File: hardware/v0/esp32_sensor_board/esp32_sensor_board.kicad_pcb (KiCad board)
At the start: 4 copper layers, 76 x 62 mm, 70 parts, among them J101 Conn_01x02, J102 Conn_01x02, J301 USB_B_Micro, J302 Micro_SD_Card_Det, J303 Conn_Coaxial, J501 Conn_01x05, J502 Conn_01x05, SW301 SW_SPST, U201 LMR36006, U302 ESP32-C3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

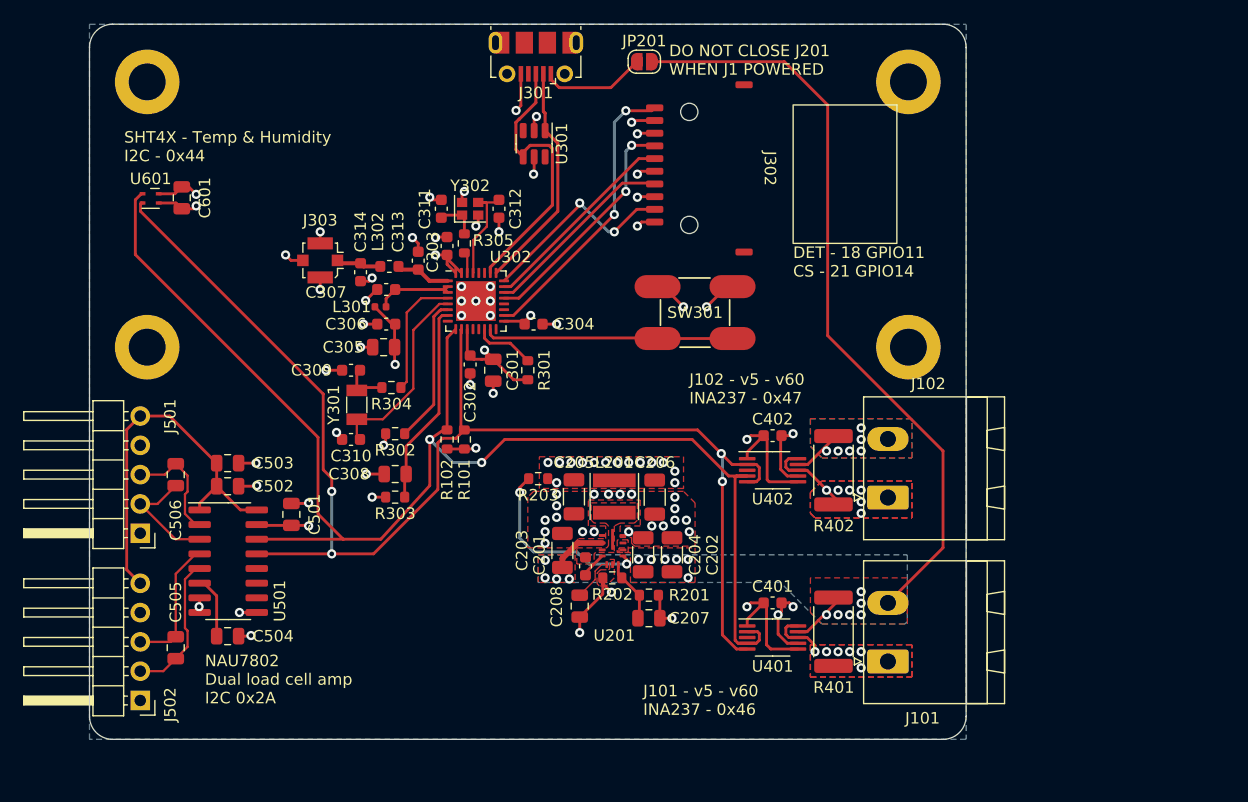
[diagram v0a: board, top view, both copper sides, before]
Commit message: Board refactor WIP.  Still needs PU resistors
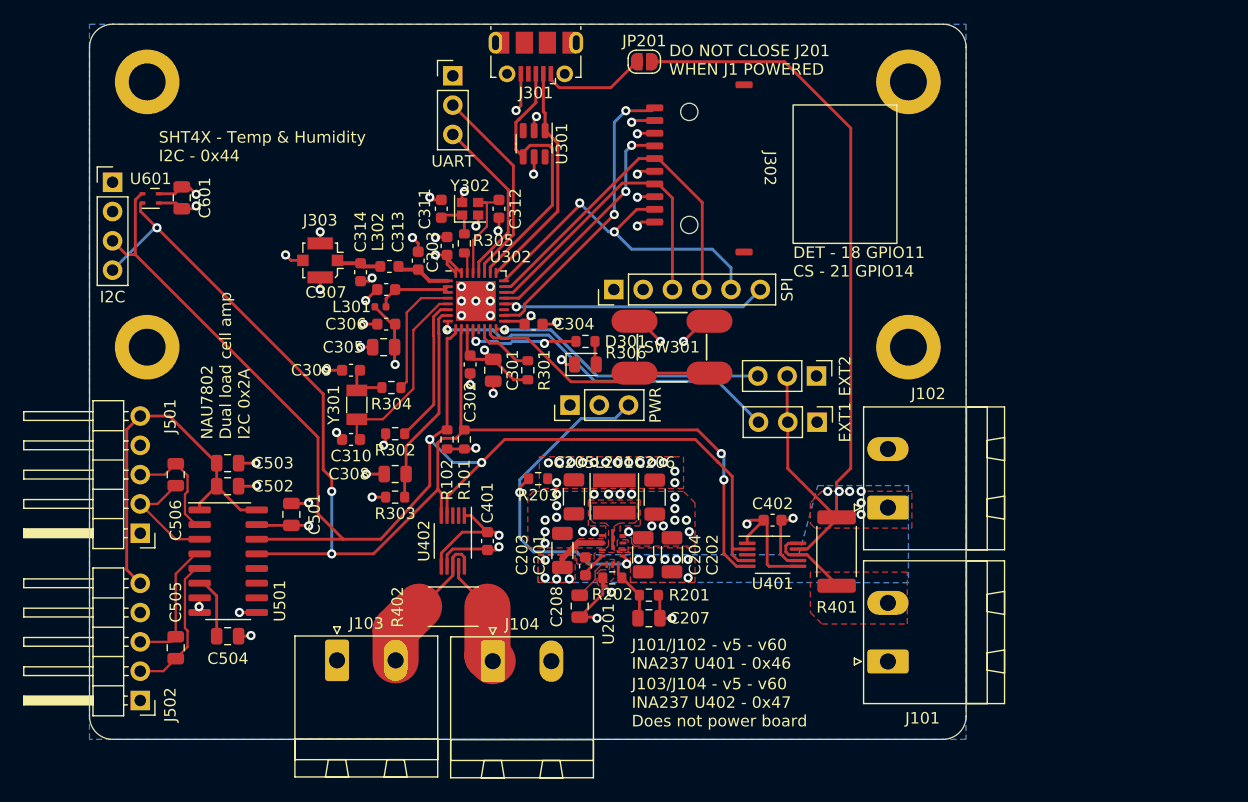
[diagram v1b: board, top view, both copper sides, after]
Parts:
- removed the G*** at (109.5, 127.0)
- added D301: STATUS_LED, LED_SMD:LED_0805_2012Metric, F.Cu at (128.5, 99.5)
- added J103: Conn_01x02, Connector_Phoenix_MSTB:PhoenixContact_MSTBA_2,5_2-G-5,08_1x02_P5.08mm_Horizontal, F.Cu at (107.0, 125.2)
- added J104: Conn_01x02, Connector_Phoenix_MSTB:PhoenixContact_MSTBA_2,5_2-G-5,08_1x02_P5.08mm_Horizontal, F.Cu at (120.5, 125.2)
- added J201: PWR, Connector_PinHeader_2.54mm:PinHeader_1x03_P2.54mm_Vertical, F.Cu at (127.2, 103.0)
- added J304: UART, Connector_PinHeader_2.54mm:PinHeader_1x03_P2.54mm_Vertical, F.Cu at (117.0, 74.5)
- added J305: EXT1, Connector_PinHeader_2.54mm:PinHeader_1x03_P2.54mm_Vertical, F.Cu at (148.6, 104.5)
- added J306: EXT2, Connector_PinHeader_2.54mm:PinHeader_1x03_P2.54mm_Vertical, F.Cu at (148.5, 100.5)
- added J307: I2C, Connector_PinHeader_2.54mm:PinHeader_1x04_P2.54mm_Vertical, F.Cu at (87.5, 83.7)
- added J308: SPI, Connector_PinHeader_2.54mm:PinHeader_1x06_P2.54mm_Vertical, F.Cu at (131.0, 93.0)
- added R306: R_Small, Resistor_SMD:R_0603_1608Metric, F.Cu at (128.5, 97.5)
- moved R402 35.0 mm to (117.0, 120.5), turned to 0 degrees
- moved U402 29.0 mm to (117.0, 114.8), turned to -90 degrees
- moved C401 25.3 mm to (120.0, 114.8), turned to -90 degrees
- moved G*** 21.4 mm to (112.5, 100.0)
- moved C402 7.33 mm to (144.7, 113.0)
- moved U401 7.33 mm to (144.7, 116.0)
- moved R401 6.96 mm to (150.3, 115.7)
- moved SW301 3.61 mm to (136.0, 98.0)
- moved J102 0.87 mm to (154.7, 111.9)
- renumbered U402 to U401, U401 to U402
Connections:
- J101 pad 1: /Vbus1_in -> GND
- J101 pad 2: VIN -> /Vbus1_in
- J102 pad 1: /Vbus2_in -> VIN
- J102 pad 2: /Vbus2_out -> GND
- U302 pad 12: unconnected-(U302-MTCK/GPIO6-Pad12) -> /Microprocessor/STATUS_LED
- U302 pad 13: unconnected-(U302-MTDO/GPIO7-Pad13) -> /Load Cell Sensor/DRDY_NAU
- U302 pad 16: unconnected-(U302-GPIO10-Pad16) -> /Microprocessor/EXT_2
- U302 pad 20: unconnected-(U302-SPIWP/GPIO13-Pad20) -> /Microprocessor/SPI_CS1
- U302 pad 27: unconnected-(U302-U0RXD/GPIO20-Pad27) -> /Microprocessor/UART_RX
- U302 pad 28: unconnected-(U302-U0TXD/GPIO21-Pad28) -> /Microprocessor/UART_TX
- U302 pad 8: unconnected-(U302-GPIO3/ADC1_CH3-Pad8) -> /Microprocessor/EXT_1
- U401 pad 10: /Vbus2_in -> /Vbus1_in
- U401 pad 2: /Power Measurement/I2C_SCL -> /Power Measurement/I2C_SDA
- U401 pad 8: /Vbus2_in -> /Vbus1_in
- U401 pad 9: /Vbus2_out -> VIN
- U402 pad 10: /Vbus1_in -> /Vbus2_in
- U402 pad 2: /Power Measurement/I2C_SDA -> /Power Measurement/I2C_SCL
- U402 pad 8: /Vbus1_in -> /Vbus2_in
- U402 pad 9: VIN -> /Vbus2_out
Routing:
- net /Microprocessor/EXT_1: track 0.00 -> 31.3 mm, vias 0 -> 1
- net /Microprocessor/EXT_2: track 0.00 -> 24.4 mm, vias 0 -> 1
- net /Microprocessor/SPI_CS1: track 0.00 -> 22.9 mm, vias 0 -> 1
- net /Microprocessor/UART_RX: track 0.00 -> 17.8 mm
- net /Microprocessor/UART_TX: track 0.00 -> 15.1 mm
- net /Microprocessor/SPI_CIPO: track 17.8 -> 31.1 mm
- net /Microprocessor/SPI_COPI: track 17.7 -> 30.9 mm
- net P_GOOD: track 16.5 -> 29.7 mm
- net /Microprocessor/STATUS_LED: track 0.00 -> 10.1 mm, vias 0 -> 2
- net /Microprocessor/SPI_SCK: track 17.0 -> 27.0 mm
- net /Vbus2_in: track 7.61 -> 13.1 mm, vias 6 -> 0
- net /Power Measurement/I2C_SCL: track 118.6 -> 113.2 mm, vias 4 -> 5
- net /Vbus2_out: track 4.35 -> 9.45 mm, vias 6 -> 0
- net /Power Measurement/I2C_SDA: track 119.3 -> 116.9 mm
- net /Vbus1_in: track 5.24 -> 7.35 mm, vias 6 -> 0
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- removed copper zone on B.Cu, net /Vbus1_in
- removed copper zone on B.Cu, net /Vbus2_in
- removed copper zone on F.Cu, net /Vbus2_in
- removed copper zone on B.Cu, net /Vbus2_out
- removed copper zone on F.Cu, net /Vbus2_out
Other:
- board text added: "ESP32-C3FH4 sensor board v5 - v60 input on J101 - Powers board v5 - v60 measurement on J103 +V is always the inside pin of each pair v0.2 Prototype - 2023-Oct-04 AB4EN"
- board text added: "J101/J102 - v5 - v60 INA237 U401 - 0x46"
- board text added: "J103/J104 - v5 - v60 INA237 U402 - 0x47 Does not power board"
- board text removed: "ESP32-C3FH4 sensor board v5 - v60 input on J101 - Powers board v5 - v60 measurement on J102 v0.1 Prototype - 2023-Jul-31"
- board text removed: "J101 - v5 - v60 INA237 - 0x46"
- board text removed: "J102 - v5 - v60 INA237 - 0x47"

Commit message: TVS and PU work
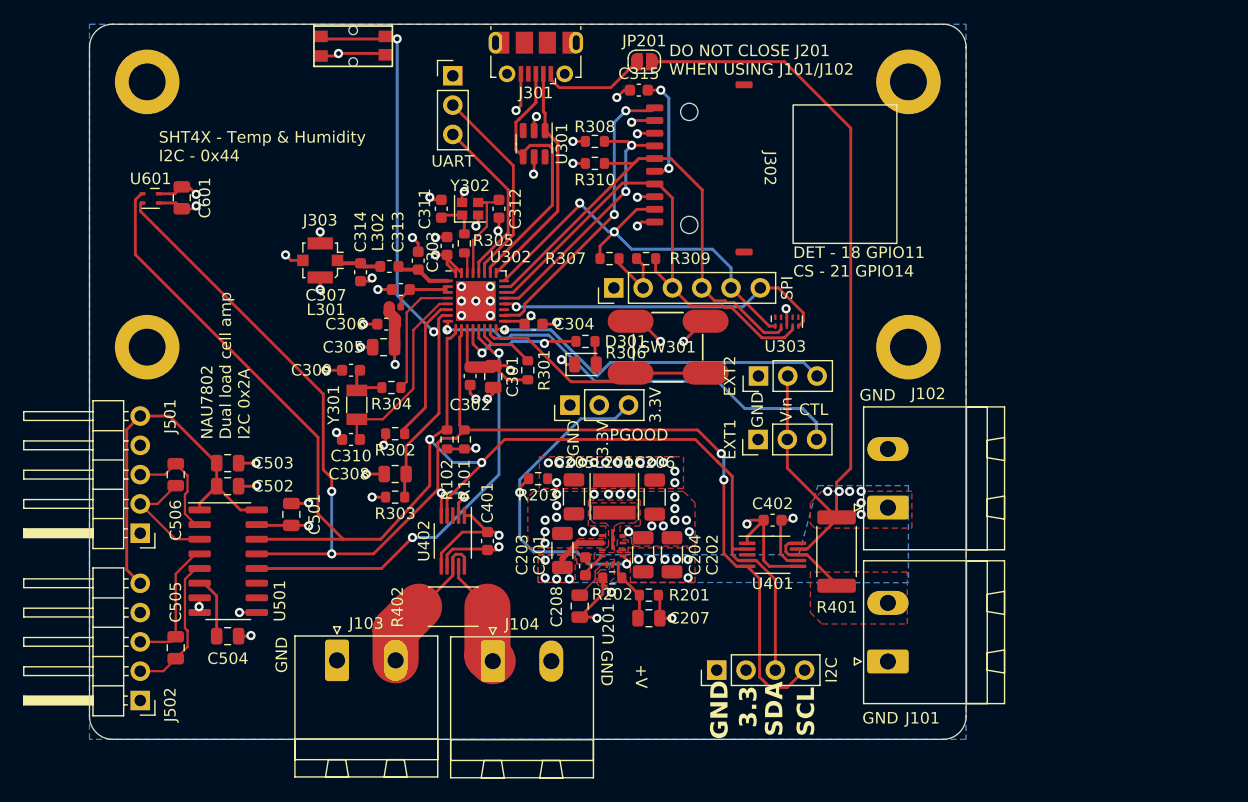
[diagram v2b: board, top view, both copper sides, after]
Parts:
- added C315: 0.1uF, Capacitor_SMD:C_0603_1608Metric, F.Cu at (133.1, 75.7)
- added R307: 50k, Resistor_SMD:R_0603_1608Metric, F.Cu at (130.6, 90.3)
- added R308: 50k, Resistor_SMD:R_0603_1608Metric, F.Cu at (129.3, 80.2)
- added R309: 50k, Resistor_SMD:R_0603_1608Metric, F.Cu at (133.8, 90.3)
- added R310: 50k, Resistor_SMD:R_0603_1608Metric, F.Cu at (129.3, 82.1)
- added SW302: RST, BVH_Switches:Tac_SMD_6.4mm_Side_SPST_NO, F.Cu at (108.4, 71.9)
- added U303: ~, BVH_Components_Misc:Diode_10Pin_DFN2510A-10_10-XFDFN_SOT1176-1, F.Cu at (146.0, 95.8)
- J201: value PWR -> 3.3V
- moved J307 67.3 mm to (139.9, 126.0), turned to 90 degrees
- moved J305 5.34 mm to (143.5, 106.0), turned to 90 degrees
- moved J306 5.03 mm to (143.5, 100.5), turned to 90 degrees
- moved C307 1.28 mm to (112.5, 93.0)
- moved L301 1.28 mm to (112.0, 94.5)
- moved C302 1.00 mm to (118.5, 100.5)
- moved C301 0.55 mm to (120.5, 100.5)
- moved SW301 0.34 mm to (135.7, 98.0)
- moved J308 0.14 mm to (131.0, 92.9)
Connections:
- J302 pad 4: +3.3V -> Net-(J302-VDD)
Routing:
- net /Load Cell Sensor/DRDY_NAU: track 0.00 -> 38.0 mm, vias 0 -> 2
- net /Microprocessor/CHIP_EN: track 17.6 -> 52.0 mm, vias 0 -> 2
- net /Microprocessor/SPI_SCK: track 27.0 -> 42.9 mm
- net /Power Measurement/I2C_SCL: track 113.2 -> 126.9 mm, vias 5 -> 6
- net /Microprocessor/SPI_COPI: track 30.9 -> 43.6 mm
- net Net-(J302-VDD): track 0.00 -> 9.49 mm, vias 0 -> 2
- net +3.3V: track 62.7 -> 71.4 mm, vias 28 -> 30
- net /Power Measurement/I2C_SDA: track 116.9 -> 125.4 mm
- net /Microprocessor/SPI_CIPO: track 31.1 -> 39.2 mm
- net GND: track 75.5 -> 83.2 mm, vias 66 -> 68
- net /Microprocessor/EXT_1: track 31.3 -> 37.8 mm
- net /Microprocessor/EXT_2: track 24.4 -> 30.5 mm
- net /Microprocessor/SPI_CS1: track 22.9 -> 28.9 mm
- net /Microprocessor/SD_CS: track 20.6 -> 23.1 mm
- net /Microprocessor/VDD33A: track 6.85 -> 5.57 mm
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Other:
- board text added: "+V"
- board text added: "3.3"
- board text added: "3.3V"
- board text added: "CTL"
- board text added: "DO NOT CLOSE J201 WHEN USING J101/J102"
- board text added: "GND"
- board text added: "PGOOD"
- board text added: "SCL"
- board text added: "SDA"
- board text added: "Vin"
- board text removed: "DO NOT CLOSE J201 WHEN J1 POWERED"

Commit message: Relay board, firmware tests
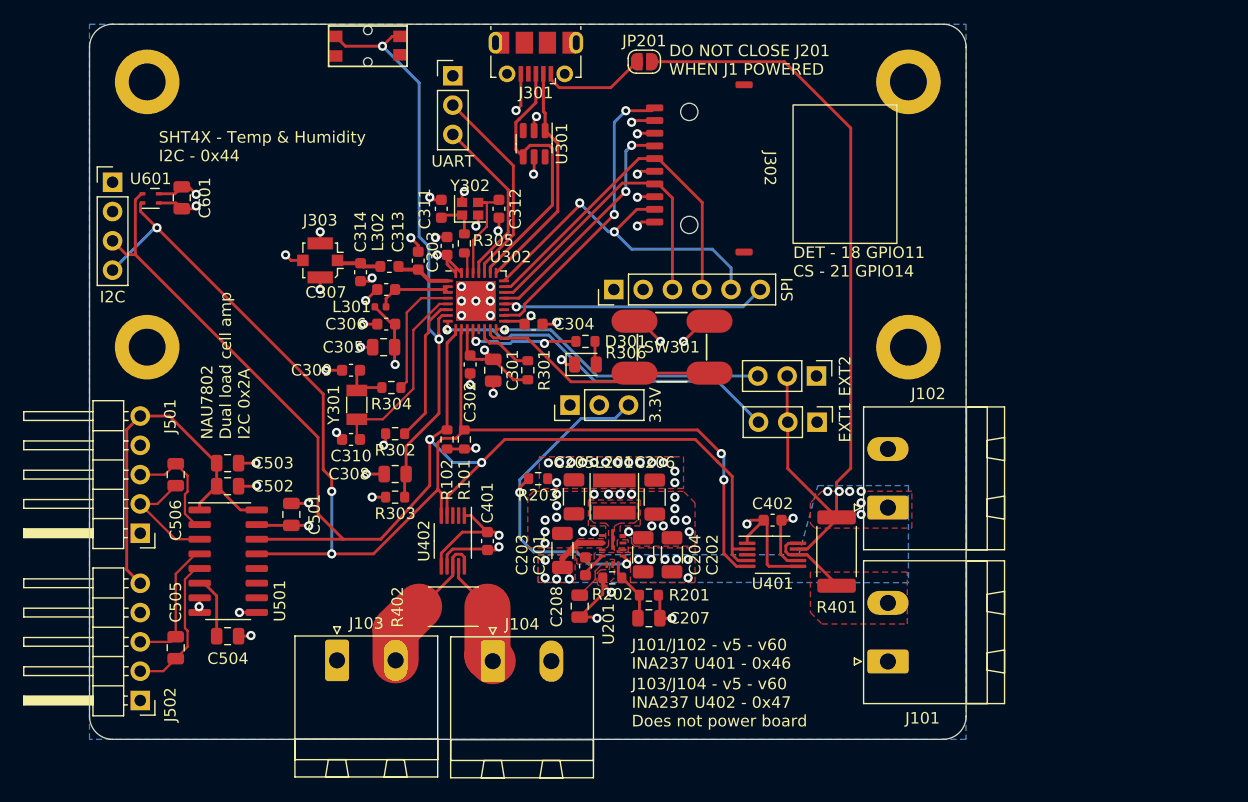
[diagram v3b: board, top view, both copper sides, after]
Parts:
- removed C315: 0.1uF, Capacitor_SMD:C_0603_1608Metric
- removed G***: LOGO, BVH_Logos:SkyIron_logo_Back
- removed R307, R308, R309, R310: 50k, Resistor_SMD:R_0603_1608Metric
- removed U303: ~, BVH_Components_Misc:Diode_10Pin_DFN2510A-10_10-XFDFN_SOT1176-1
- moved J307 67.3 mm to (87.5, 83.7), turned to 0 degrees
- moved J305 5.34 mm to (148.6, 104.5), turned to -90 degrees
- moved J306 5.03 mm to (148.5, 100.5), turned to -90 degrees
- moved C307 1.28 mm to (111.2, 93.0)
- moved L301 1.28 mm to (110.7, 94.5)
- moved SW302 1.27 mm to (109.6, 71.9)
- moved C302 1.00 mm to (118.5, 99.5)
- moved C301 0.55 mm to (120.5, 100.0)
- moved SW301 0.34 mm to (136.0, 98.0)
- moved J308 0.14 mm to (131.0, 93.0)
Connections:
- J302 pad 4: Net-(J302-VDD) -> +3.3V
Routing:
- net /Load Cell Sensor/DRDY_NAU: track 38.0 -> 0.00 mm, vias 2 -> 0
- net /Microprocessor/SPI_SCK: track 42.9 -> 27.0 mm
- net /Power Measurement/I2C_SCL: track 126.9 -> 113.2 mm, vias 6 -> 5
- net /Microprocessor/SPI_COPI: track 43.6 -> 30.9 mm
- net Net-(J302-VDD): track 9.49 -> 0.00 mm, vias 2 -> 0
- net +3.3V: track 71.4 -> 62.6 mm, vias 30 -> 28
- net /Power Measurement/I2C_SDA: track 125.4 -> 116.7 mm
- net /Microprocessor/SPI_CIPO: track 39.2 -> 31.1 mm
- net GND: track 83.2 -> 75.5 mm, vias 68 -> 66
- net /Microprocessor/EXT_1: track 37.8 -> 31.3 mm
- net /Microprocessor/EXT_2: track 30.5 -> 24.4 mm
- net /Microprocessor/SPI_CS1: track 28.9 -> 22.9 mm
- net /Microprocessor/SD_CS: track 23.1 -> 20.6 mm
- net /Microprocessor/VDD33A: track 5.57 -> 6.85 mm
- net /Microprocessor/STATUS_LED: track 11.1 -> 10.1 mm
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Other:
- board text added: "DO NOT CLOSE J201 WHEN J1 POWERED"
- board text removed: "+V"
- board text removed: "3.3"
- board text removed: "3.3V"
- board text removed: "CTL"
- board text removed: "DO NOT CLOSE J201 WHEN USING J101/J102"
- board text removed: "GND"
- board text removed: "PGOOD"
- board text removed: "SCL"
- board text removed: "SDA"
- board text removed: "Vin"

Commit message: WIP v3 hardware
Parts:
- added C315: 0.1uF, Capacitor_SMD:C_0603_1608Metric, F.Cu at (178.2, 80.4)
- added R307: 50k, Resistor_SMD:R_0603_1608Metric, F.Cu at (178.2, 83.0)
- added R308: 50k, Resistor_SMD:R_0603_1608Metric, F.Cu at (178.2, 85.5)
- added R309: 50k, Resistor_SMD:R_0603_1608Metric, F.Cu at (178.2, 88.0)
- added R310: 50k, Resistor_SMD:R_0603_1608Metric, F.Cu at (178.2, 90.5)
- added R311: 5.1k, Resistor_SMD:R_0603_1608Metric, F.Cu at (178.2, 93.0)
- added R312: 5.1k, Resistor_SMD:R_0603_1608Metric, F.Cu at (178.2, 95.5)
- added U303: ~, BVH_Components_Misc:Diode_10Pin_DFN2510A-10_10-XFDFN_SOT1176-1, F.Cu at (181.7, 81.2)
- C313, C314: value C_Small -> 2.1pF
- JP201: value Jumper_2_Open -> USB Power Jumper; footprint Jumper:SolderJumper-2_P1.3mm_Open_RoundedPad1.0x1.5mm -> Jumper:SolderJumper-2_P1.3mm_Bridged_RoundedPad1.0x1.5mm
- L302: value L_Small -> 5.6nH
- SW301: value SW_SPST -> BOOT
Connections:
- J302 pad 4: +3.3V -> Net-(J302-VDD)
- JP201 pad 2: VIN -> Net-(D1-A)
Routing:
- net +3.3V: track 62.6 -> 61.0 mm, vias 28 -> 27
- net Net-(J302-VDD): track 0.00 -> 1.60 mm, vias 0 -> 1
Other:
- board text removed: "DO NOT CLOSE J201 WHEN J1 POWERED"

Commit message: WIP
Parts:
- added D1: D_Small, Diode_SMD:D_SOD-123, F.Cu at (147.2, 73.0)
- added G***: LOGO, BVH_Logos:SkyIron_logo_Back, F.Cu at (106.1, 114.5)
- J201: value 3.3V -> PWR
- J301: value USB_B_Micro -> USB4510-03-1-A_REVA; footprint Connector_USB:USB_Micro-B_Molex-105017-0001 -> USB4510-03-1-A:GCT_USB4510-03-1-A_REVA
- moved R312 58.5 mm to (122.0, 79.2)
- moved R311 50.6 mm to (129.2, 80.0), turned to 180 degrees
- moved U303 45.0 mm to (137.5, 89.9), turned to 90 degrees
- moved C315 43.9 mm to (134.5, 84.5), turned to -90 degrees
- moved R310 42.9 mm to (136.2, 81.5), turned to -90 degrees
- moved R309 42.1 mm to (136.2, 84.5), turned to 90 degrees
- moved R308 40.1 mm to (138.2, 81.5), turned to -90 degrees
- moved R307 40.0 mm to (138.2, 84.5), turned to 90 degrees
- moved JP201 8.40 mm to (142.0, 73.0)
- moved J302 5.98 mm to (140.8, 83.8)
- moved C601 5.26 mm to (98.8, 84.8)
- moved U601 4.45 mm to (95.2, 85.1)
- moved U301 1.77 mm to (125.7, 81.0)
- moved J301 1.54 mm to (125.1, 71.6)
- moved C302 0.75 mm to (118.5, 100.2)
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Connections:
- C315 pad 1: +3.3V -> GND
- C315 pad 2: Net-(J302-VDD) -> +3.3V
- J302 pad 4: Net-(J302-VDD) -> +3.3V
- U303 pad 1: /Microprocessor/SPI_CIPO -> /Microprocessor/SPI_SCK
- U303 pad 4: /Microprocessor/SPI_SCK -> /Microprocessor/SPI_CIPO
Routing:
- net /Load Cell Sensor/DRDY_NAU: track 0.00 -> 36.5 mm, vias 0 -> 2
- net +3.3V: track 61.0 -> 78.7 mm, vias 27 -> 31
- net VIN: track 77.3 -> 65.3 mm
- net /Microprocessor/SPI_CIPO: track 31.1 -> 42.9 mm
- net /Microprocessor/SPI_COPI: track 30.9 -> 42.6 mm, vias 0 -> 3
- net GND: track 75.5 -> 85.3 mm, vias 66 -> 70
- net /Microprocessor/SPI_SCK: track 27.0 -> 35.8 mm, vias 0 -> 2
- net +5V: track 9.16 -> 16.9 mm
- net /Microprocessor/SD_CS: track 20.6 -> 27.4 mm
- net /Microprocessor/USB_P: track 24.5 -> 17.8 mm
- net /Microprocessor/SPI_CS1: track 22.9 -> 29.2 mm
- net /Microprocessor/SD_DET: track 25.5 -> 31.8 mm
- net Net-(J301-CC1): track 0.00 -> 4.10 mm
- net Net-(D1-A): track 0.00 -> 2.95 mm
- net Net-(J301-CC2): track 0.00 -> 2.73 mm
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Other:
- outline, holes or cut-outs redrawn
- board text added: "+5V - 60V"
- board text added: "3.3"
- board text added: "3.3V"
- board text added: "A: 0x44"
- board text added: "AB4EN"
- board text added: "B: 0x45"
- board text added: "CIPO"
- board text added: "COPI"
- board text added: "CS1 GPIO14"
- board text added: "DET - GPIO11 CS - GPIO14"
- board text added: "E+/RD"
- board text added: "E-/BK"
- board text added: "ESP32-C3FH4 sensor board v0.3 Prototype - 2024-Jul-18"
- board text added: "EXT1 GPIO03-ADC"
- board text added: "EXT2 GPIO04"
- board text added: "GND"
- board text added: "GND/Y"
- board text added: "J101/102 Board & Sense U401 - 0x46"
- board text added: "J103/104 Sense Only U401 - 0x47"
- board text added: "LOAD"
- board text added: "NAU7802 0x2A"
- board text added: "PGD"
- board text added: "RX"
- board text added: "S+/GN"
- board text added: "S-/WT"
- board text added: "SCK"
- board text added: "SCK: GPIO15 COPI: GPIO16 CIPO: GPIO17"
- board text added: "SCL"
- board text added: "SDA"
- board text added: "SHT4X I2C T RH"
- board text added: "SRC"
- board text added: "TX"
- board text added: "VIN"
- board text removed: "DET - 18 GPIO11 CS - 21 GPIO14"
- board text removed: "ESP32-C3FH4 sensor board v5 - v60 input on J101 - Powers board v5 - v60 measurement on J103 +V is always the inside pin of each pair v0.2 Prototype - 2023-Oct-04 AB4EN"
- board text removed: "J101/J102 - v5 - v60 INA237 U401 - 0x46"
- board text removed: "J103/J104 - v5 - v60 INA237 U402 - 0x47 Does not power board"
- board text removed: "NAU7802 Dual load cell amp I2C 0x2A"
- board text removed: "SHT4X - Temp & Humidity I2C - 0x44"
